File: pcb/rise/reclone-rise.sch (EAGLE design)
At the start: 12 parts, among them J1 MAGJACK, U1 6SLX16FTG256

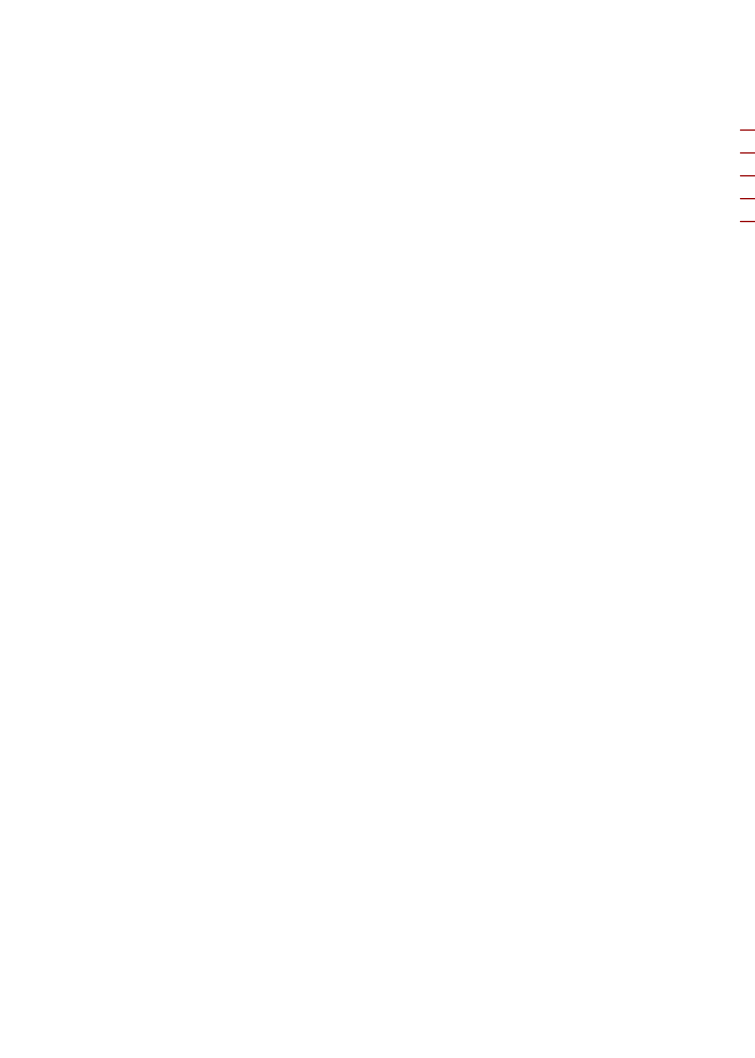
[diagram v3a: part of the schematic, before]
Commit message: Finished a basic DDR2 SDRAM part
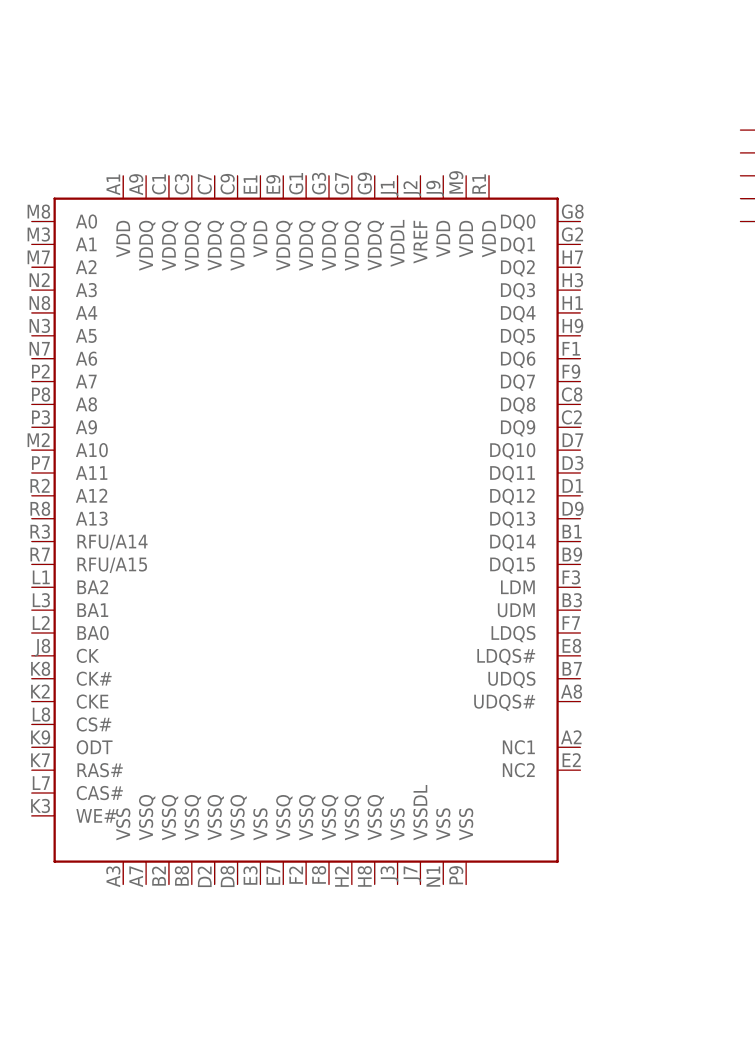
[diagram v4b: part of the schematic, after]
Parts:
- added U$5: MT47H128M16, reclone-rise:MT47H128M16
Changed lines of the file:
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@@
 <part name="U1" library="xilinx_devices_V6" deviceset="6SLX16FTG256" device=""/>
 <part name="U$4" library="Gadgeteer" deviceset="SHF105" device=""/>
+<part name="U$5" library="reclone-rise" deviceset="MT47H128M16" device=""/>
 </parts>
 <sheets>
@@
 <instance part="U1" gate="B0" x="-7.62" y="73.66"/>
 <instance part="U$4" gate="X" x="-63.5" y="147.32"/>
+<instance part="U$5" gate="G$1" x="-121.92" y="106.68"/>
 </instances>
 <busses>

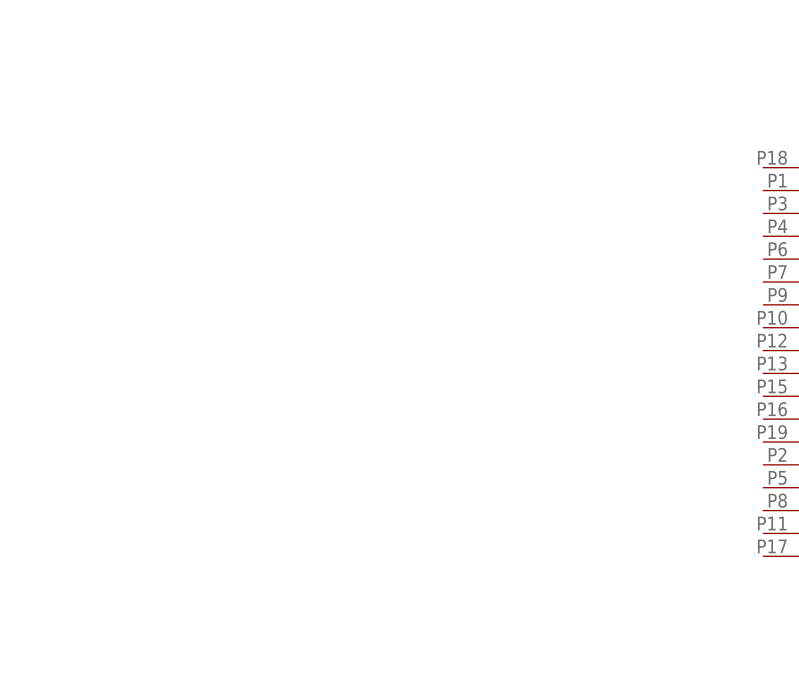
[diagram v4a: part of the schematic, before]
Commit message: Added microSD socket as a placeholder
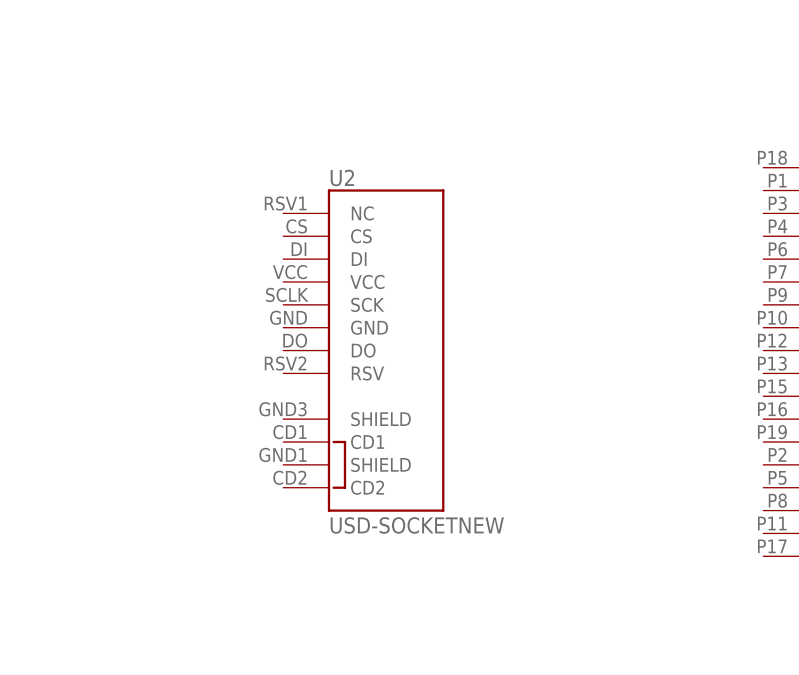
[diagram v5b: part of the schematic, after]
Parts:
- added U2: USD-SOCKETNEW, SparkFun-Connectors:USD-SOCKETNEW
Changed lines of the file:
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@@
 <part name="U$4" library="Gadgeteer" deviceset="SHF105" device=""/>
 <part name="U$5" library="reclone-rise" deviceset="MT47H128M16" device=""/>
+<part name="U2" library="SparkFun-Connectors" deviceset="USD-SOCKET" device="NEW"/>
 </parts>
 <sheets>
@@
 <instance part="U$4" gate="X" x="-63.5" y="147.32"/>
 <instance part="U$5" gate="G$1" x="-121.92" y="106.68"/>
+<instance part="U2" gate="G$1" x="-116.84" y="30.48"/>
 </instances>
 <busses>

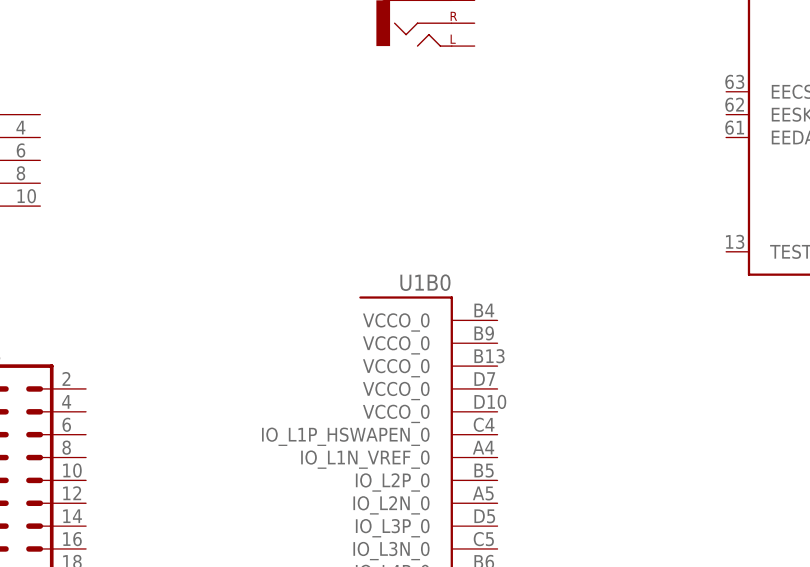
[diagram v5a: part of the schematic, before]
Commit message: Added draft FPC15-0.5 package for FPC vertical mount connector for camera and lcd
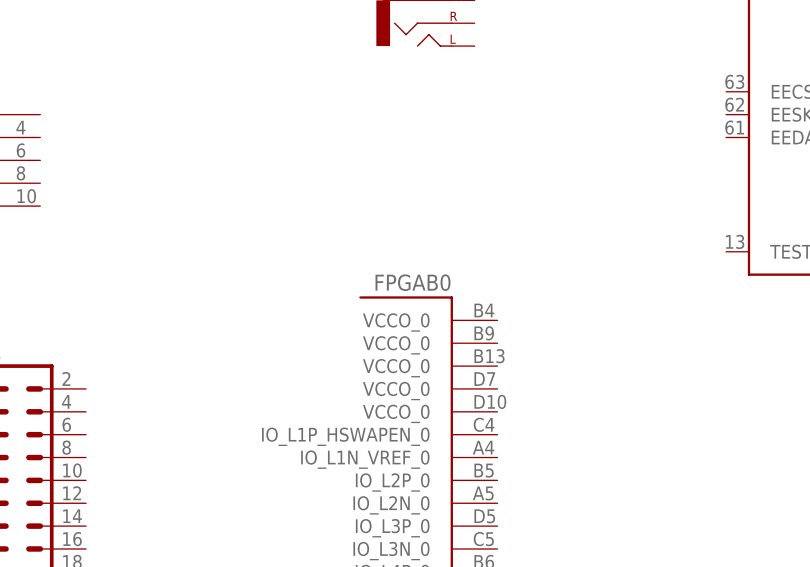
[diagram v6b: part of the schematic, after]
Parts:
- renumbered U1 to FPGA
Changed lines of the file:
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@@
 <part name="U$2" library="reclone-rise" deviceset="DP83848C" device=""/>
 <part name="U$3" library="reclone-rise" deviceset="HDMI_A" device=""/>
-<part name="U1" library="xilinx_devices_V6" deviceset="6SLX16FTG256" device=""/>
+<part name="FPGA" library="xilinx_devices_V6" deviceset="6SLX16FTG256" device=""/>
 <part name="U$4" library="Gadgeteer" deviceset="SHF105" device=""/>
 <part name="U$5" library="reclone-rise" deviceset="MT47H128M16" device=""/>
@@
 <instance part="U$2" gate="G$1" x="-33.02" y="228.6"/>
 <instance part="U$3" gate="G$1" x="-55.88" y="27.94"/>
-<instance part="U1" gate="B0" x="-7.62" y="73.66"/>
+<instance part="FPGA" gate="B0" x="-7.62" y="73.66"/>
 <instance part="U$4" gate="X" x="-63.5" y="147.32"/>
 <instance part="U$5" gate="G$1" x="-121.92" y="106.68"/>

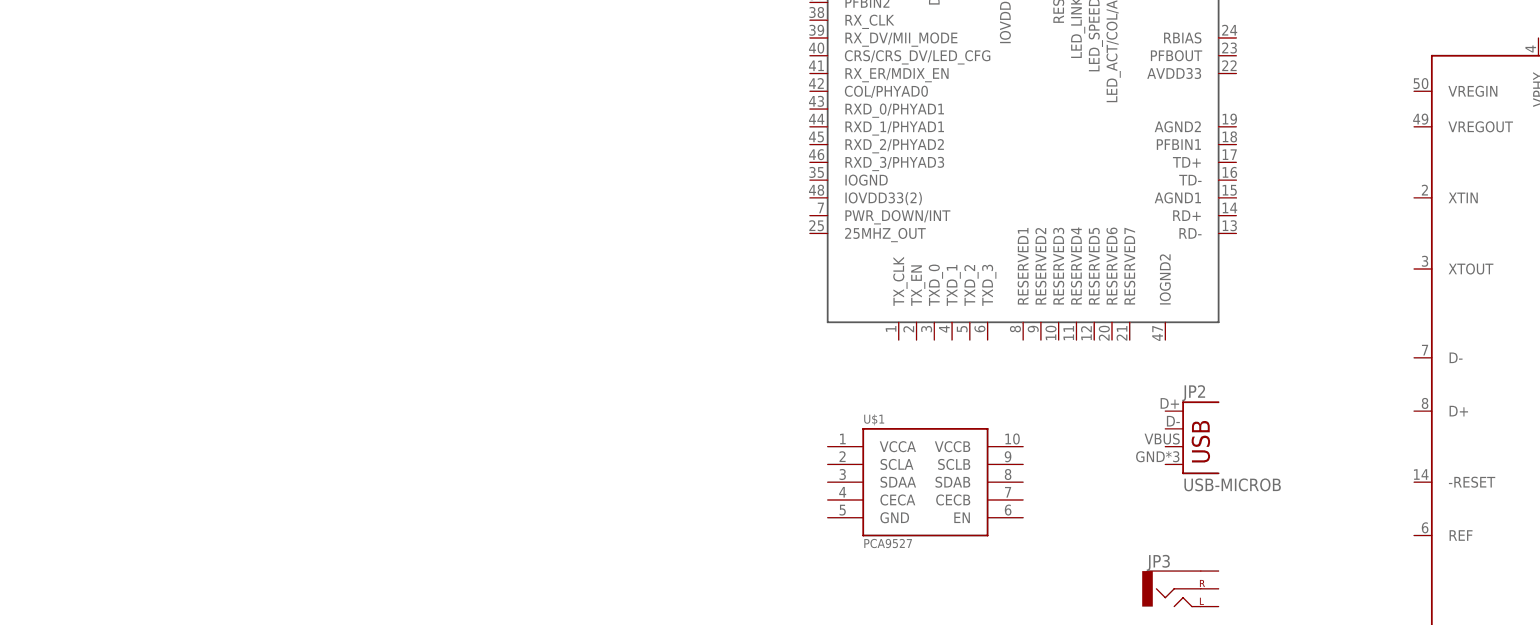
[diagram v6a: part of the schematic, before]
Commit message: Added LCD and camera connectors to the board
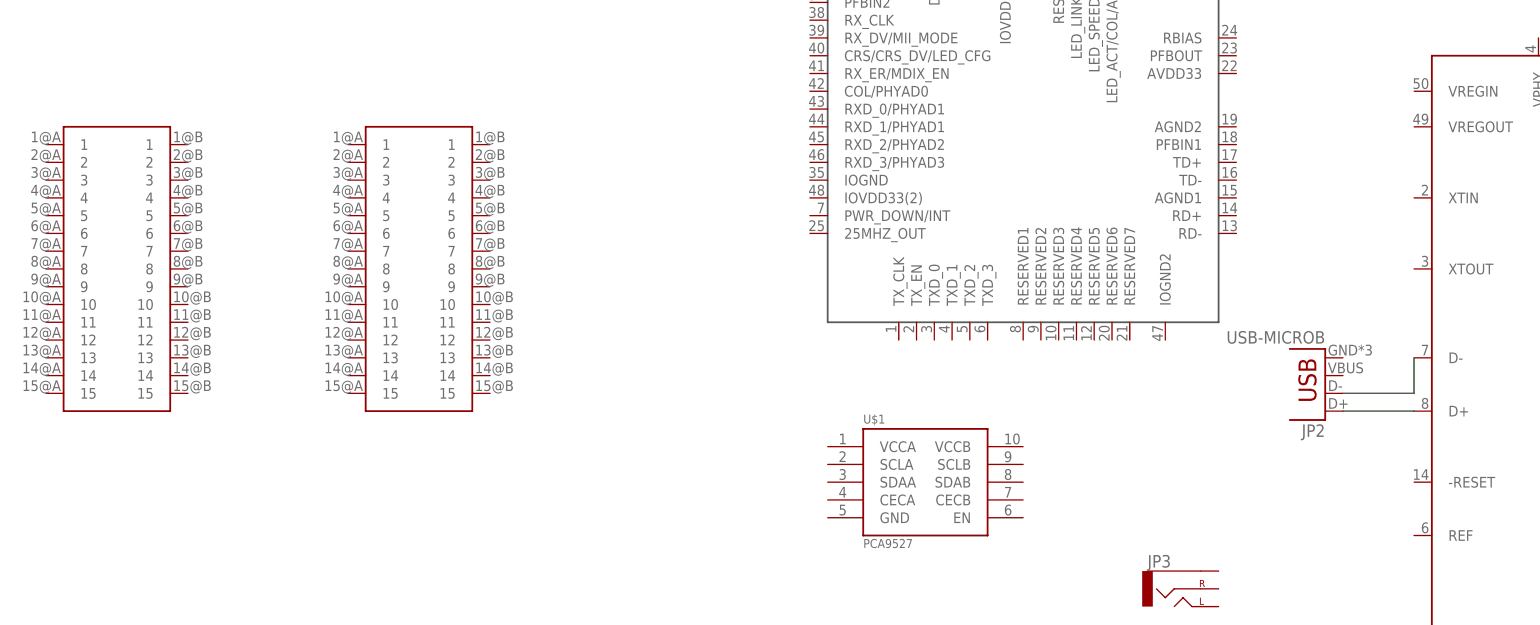
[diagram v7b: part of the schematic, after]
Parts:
- added U$8, U$9: FPC15-1.0, reclone-rise:FPC15-1.0
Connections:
- new net N$1: IC1.D+, JP2.D+
- new net N$2: IC1.D-, JP2.D-
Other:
- moved on the sheet: JP2
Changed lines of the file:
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@@
 <part name="U$5" library="reclone-rise" deviceset="MT47H128M16" device=""/>
 <part name="U2" library="SparkFun-Connectors" deviceset="USD-SOCKET" device="NEW"/>
+<part name="U$8" library="reclone-rise" deviceset="FPC15-1.0" device=""/>
+<part name="U$9" library="reclone-rise" deviceset="FPC15-1.0" device=""/>
 </parts>
 <sheets>
@@
 <instance part="J1" gate="G$1" x="38.1" y="81.28"/>
 <instance part="IC1" gate="G$1" x="55.88" y="193.04"/>
-<instance part="JP2" gate="G$1" x="-10.16" y="180.34"/>
+<instance part="JP2" gate="G$1" x="10.16" y="195.58" rot="R180"/>
 <instance part="JP3" gate="G$1" x="-10.16" y="162.56"/>
 <instance part="U$1" gate="G$1" x="-45.72" y="177.8"/>
@@
 <instance part="U$5" gate="G$1" x="-121.92" y="106.68"/>
 <instance part="U2" gate="G$1" x="-116.84" y="30.48"/>
+<instance part="U$8" gate="G$1" x="-165.1" y="208.28"/>
+<instance part="U$9" gate="G$1" x="-121.92" y="208.28"/>
 </instances>
 <busses>
 </busses>
 <nets>
+<net name="N$1" class="0">
+<segment>
+<pinref part="JP2" gate="G$1" pin="D+"/>
+<pinref part="IC1" gate="G$1" pin="D+"/>
+<wire x1="12.7" y1="187.96" x2="22.86" y2="187.96" width="0.1524" layer="91"/>
+</segment>
+</net>
+<net name="N$2" class="0">
+<segment>
+<pinref part="JP2" gate="G$1" pin="D-"/>
+<pinref part="IC1" gate="G$1" pin="D-"/>
+<wire x1="12.7" y1="190.5" x2="22.86" y2="190.5" width="0.1524" layer="91"/>
+<wire x1="22.86" y1="190.5" x2="22.86" y2="195.58" width="0.1524" layer="91"/>
+</segment>
+</net>
 </nets>
 </sheet>

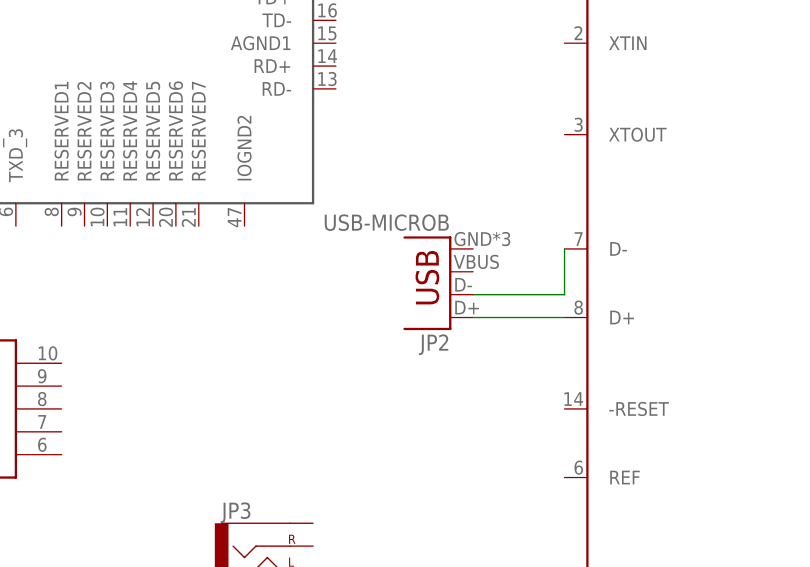
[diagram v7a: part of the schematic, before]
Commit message: Updated Micro USB connector to a cheap one that has thru hole anchors; Added some part numbers to BOM
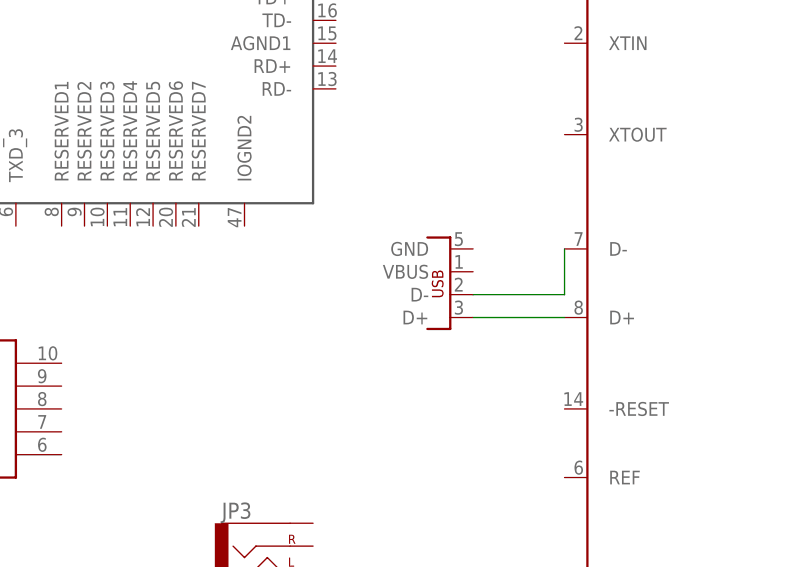
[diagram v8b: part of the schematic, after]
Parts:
- removed JP2: USB-MICROB, SparkFun-Connectors:USB-MICROB
- added U$6: USB-MICRO-B-SMD, reclone-rise:USB-MICRO-B-SMD
- U$3: DIGIKEY# (none) -> 609-4614-1-ND; MANF (none) -> FCI; MANF# (none) -> 10029449-111RLF
- U$8, U$9: DIGIKEY# (none) -> WM11008CT-ND; MANF (none) -> Molex; MANF# (none) -> 0526101572
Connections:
- net N$1: now also U$6.D+; no longer JP2.D+
- net N$2: now also U$6.D-; no longer JP2.D-
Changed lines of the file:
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@@
 <part name="J1" library="SparkFun-Connectors" deviceset="MAGJACK" device=""/>
 <part name="IC1" library="ftdichip-3" deviceset="FT2232H" device="L"/>
-<part name="JP2" library="SparkFun-Connectors" deviceset="USB" device="-MICROB"/>
 <part name="JP3" library="SparkFun-Connectors" deviceset="AUDIO-JACK" device="SMD2"/>
 <part name="U$1" library="reclone-rise" deviceset="PCA9527" device=""/>
 <part name="U$2" library="reclone-rise" deviceset="DP83848C" device=""/>
-<part name="U$3" library="reclone-rise" deviceset="HDMI_A" device=""/>
+<part name="U$3" library="reclone-rise" deviceset="HDMI_A" device="">
+<attribute name="DIGIKEY#" value="609-4614-1-ND"/>
+<attribute name="MANF" value="FCI"/>
+<attribute name="MANF#" value="10029449-111RLF"/>
+</part>
 <part name="FPGA" library="xilinx_devices_V6" deviceset="6SLX16FTG256" device=""/>
 <part name="U$4" library="Gadgeteer" deviceset="SHF105" device=""/>
 <part name="U$5" library="reclone-rise" deviceset="MT47H128M16" device=""/>
 <part name="U2" library="SparkFun-Connectors" deviceset="USD-SOCKET" device="NEW"/>
-<part name="U$8" library="reclone-rise" deviceset="FPC15-1.0" device=""/>
-<part name="U$9" library="reclone-rise" deviceset="FPC15-1.0" device=""/>
+<part name="U$8" library="reclone-rise" deviceset="FPC15-1.0" device="">
+<attribute name="DIGIKEY#" value="WM11008CT-ND"/>
+<attribute name="MANF" value="Molex"/>
+<attribute name="MANF#" value="0526101572"/>
+</part>
+<part name="U$9" library="reclone-rise" deviceset="FPC15-1.0" device="">
+<attribute name="DIGIKEY#" value="WM11008CT-ND"/>
+<attribute name="MANF" value="Molex"/>
+<attribute name="MANF#" value="0526101572"/>
+</part>
+<part name="U$6" library="reclone-rise" deviceset="USB-MICRO-B-SMD" device="">
+<attribute name="DIGIKEY#" value="609-4618-1-ND"/>
+<attribute name="MANF" value="FCI"/>
+<attribute name="MANF#" value="10118194-0001LF"/>
+</part>
 </parts>
 <sheets>
@@
 <instance part="J1" gate="G$1" x="38.1" y="81.28"/>
 <instance part="IC1" gate="G$1" x="55.88" y="193.04"/>
-<instance part="JP2" gate="G$1" x="10.16" y="195.58" rot="R180"/>
 <instance part="JP3" gate="G$1" x="-10.16" y="162.56"/>
 <instance part="U$1" gate="G$1" x="-45.72" y="177.8"/>
 <instance part="U$2" gate="G$1" x="-33.02" y="228.6"/>
-<instance part="U$3" gate="G$1" x="-55.88" y="27.94"/>
+<instance part="U$3" gate="G$1" x="-55.88" y="27.94">
+<attribute name="MANF" x="-55.88" y="27.94" size="1.778" layer="96" display="off"/>
+<attribute name="DIGIKEY#" x="-55.88" y="27.94" size="1.778" layer="96" display="off"/>
+<attribute name="MANF#" x="-55.88" y="27.94" size="1.778" layer="96" display="off"/>
+</instance>
 <instance part="FPGA" gate="B0" x="-7.62" y="73.66"/>
 <instance part="U$4" gate="X" x="-63.5" y="147.32"/>
 <instance part="U$5" gate="G$1" x="-121.92" y="106.68"/>
 <instance part="U2" gate="G$1" x="-116.84" y="30.48"/>
-<instance part="U$8" gate="G$1" x="-165.1" y="208.28"/>
-<instance part="U$9" gate="G$1" x="-121.92" y="208.28"/>
+<instance part="U$8" gate="G$1" x="-165.1" y="208.28">
+<attribute name="MANF" x="-165.1" y="208.28" size="1.778" layer="96" display="off"/>
+<attribute name="DIGIKEY#" x="-165.1" y="208.28" size="1.778" layer="96" display="off"/>
+<attribute name="MANF#" x="-165.1" y="208.28" size="1.778" layer="96" display="off"/>
+</instance>
+<instance part="U$9" gate="G$1" x="-121.92" y="208.28">
+<attribute name="DIGIKEY#" x="-121.92" y="208.28" size="1.778" layer="96" display="off"/>
+<attribute name="MANF" x="-121.92" y="208.28" size="1.778" layer="96" display="off"/>
+<attribute name="MANF#" x="-121.92" y="208.28" size="1.778" layer="96" display="off"/>
+</instance>
+<instance part="U$6" gate="G$1" x="10.16" y="195.58" rot="R180">
+<attribute name="DIGIKEY#" x="10.16" y="195.58" size="1.778" layer="96" rot="R180" display="off"/>
+<attribute name="MANF" x="10.16" y="195.58" size="1.778" layer="96" rot="R180" display="off"/>
+<attribute name="MANF#" x="10.16" y="195.58" size="1.778" layer="96" rot="R180" display="off"/>
+</instance>
 </instances>
 <busses>
@@
 <net name="N$1" class="0">
 <segment>
-<pinref part="JP2" gate="G$1" pin="D+"/>
 <pinref part="IC1" gate="G$1" pin="D+"/>
 <wire x1="12.7" y1="187.96" x2="22.86" y2="187.96" width="0.1524" layer="91"/>
+<pinref part="U$6" gate="G$1" pin="D+"/>
 </segment>
 </net>
 <net name="N$2" class="0">
 <segment>
-<pinref part="JP2" gate="G$1" pin="D-"/>
 <pinref part="IC1" gate="G$1" pin="D-"/>
 <wire x1="12.7" y1="190.5" x2="22.86" y2="190.5" width="0.1524" layer="91"/>
 <wire x1="22.86" y1="190.5" x2="22.86" y2="195.58" width="0.1524" layer="91"/>
+<pinref part="U$6" gate="G$1" pin="D-"/>
 </segment>
 </net>
